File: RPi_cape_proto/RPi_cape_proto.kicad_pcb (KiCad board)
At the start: 2 copper layers, 104 x 172 mm, 206 parts, among them J1 Conn_01x04, J10 Conn_01x02, J11 Conn_01x02, J12 Conn_01x02, J14 Conn_01x02, J15 Conn_01x06, J16 Conn_01x06, J2 Conn_02x20_Odd_Even, J21 Conn_01x06, J3 Conn_01x02, J4 Conn_01x02, J5 Conn_02x20_Odd_Even, J7 Conn_01x02, J8 Conn_02x20_Odd_Even, J9 Conn_01x02, Q1 MMBT3904, Q11 MMBT3904, Q12 MMBT3906, Q13 MMBT3904, Q2 MMBT3904, Q3 MMBT3904, U18 74LVC1G08, U19 TPS1H100B, U2 ADC128D818, U20 74LVC1G08, U21 TPS1H100B, U22 74LVC1G08, U23 TPS1H100B, U28 LM4871M, U3 ADC128D818, U36 LMC7101B, U37 LMC7101B, U38 LMC7101B, U4 AD8552A, U8 74LVC1G08, U9 TPS1H100B

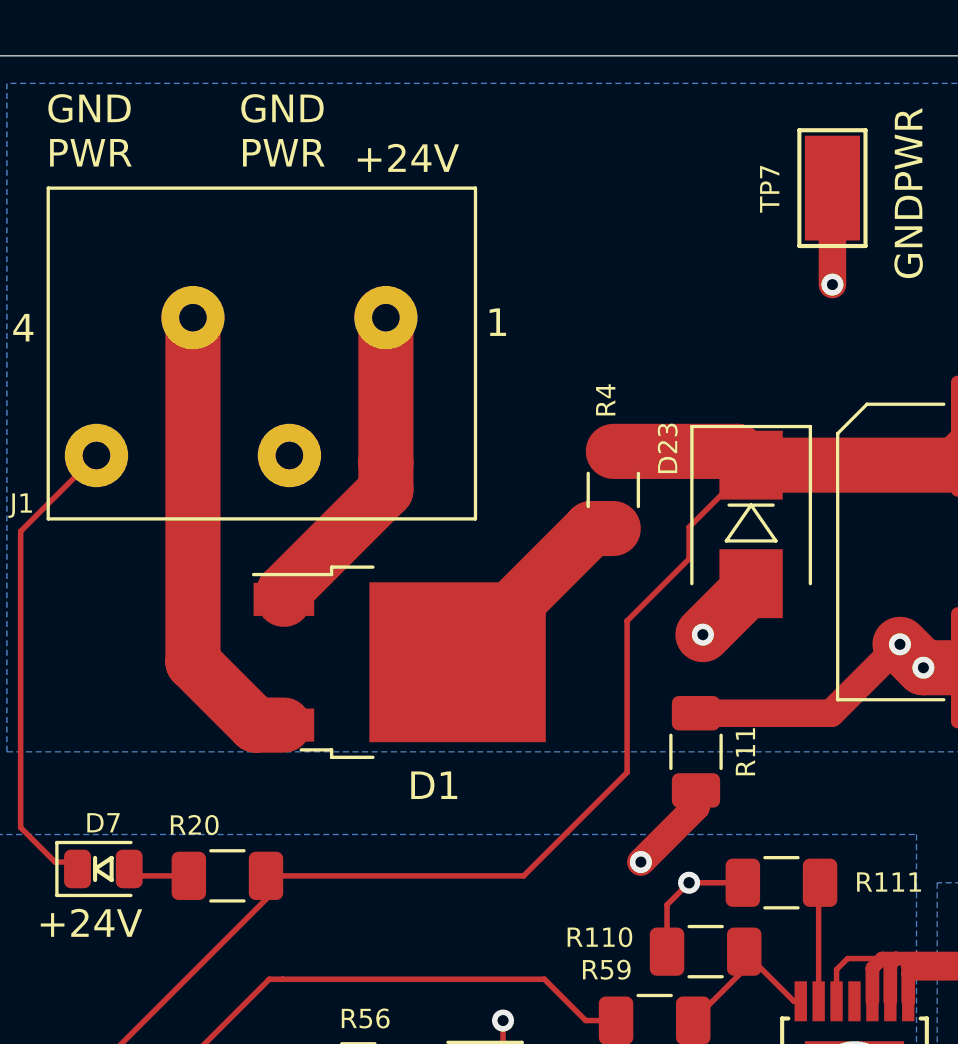
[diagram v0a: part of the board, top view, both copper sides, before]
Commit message: Input ORing-diode details
Changed part number and improved heatsinking for input power OR-ing diode
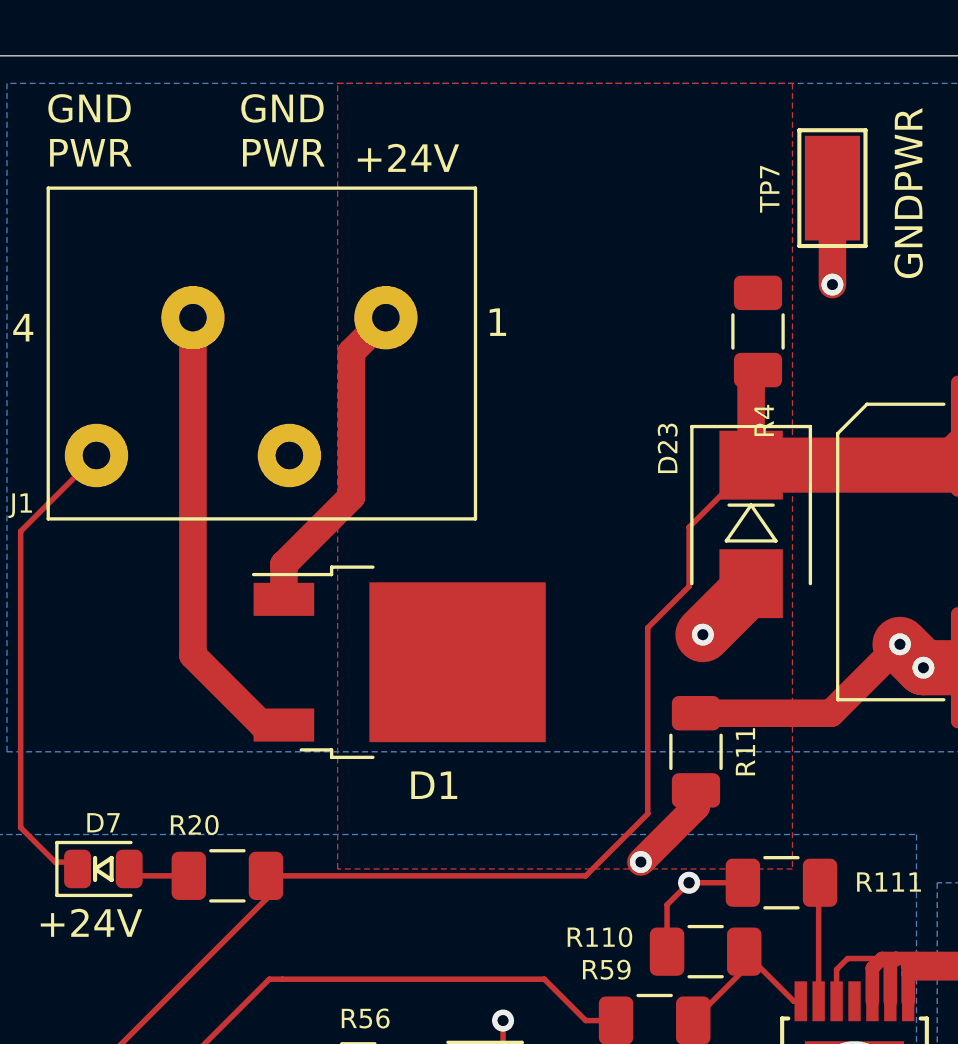
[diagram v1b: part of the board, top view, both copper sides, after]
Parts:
- moved R4 7.79 mm to (108.2, 121.5), turned to 270 degrees
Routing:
- net Net-(D1-Pad2): track 7.66 -> 0.00 mm
- added copper zone on F.Cu, net Net-(D1-Pad2)
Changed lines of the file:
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@@
     (thickness 1.6)
     (drawings 56)
-    (tracks 1412)
+    (tracks 1410)
     (zones 0)
     (modules 206)
@@
   )
   (setup
-    (last_trace_width 0.2)
+    (last_trace_width 1)
     (user_trace_width 0.2)
     (user_trace_width 0.25)
@@
     (mod_text_size 1 1)
     (mod_text_width 0.15)
-    (pad_size 5.35 8.54)
+    (pad_size 6.4 5.8)
     (pad_drill 0)
     (pad_to_mask_clearance 0.051)
@@
     (pad "" smd rect (at 3.775 1.525) (size 3.05 2.75) (layers F.Paste))
     (pad 2 smd rect (at 2.1 0) (size 6.4 5.8) (layers F.Cu F.Mask)
-      (net 27 "Net-(D1-Pad2)"))
+      (net 27 "Net-(D1-Pad2)") (zone_connect 2))
     (pad 3 smd rect (at -4.2 2.28) (size 2.2 1.2) (layers F.Cu F.Paste F.Mask)
       (net 209 "Net-(D1-Pad3)"))
@@
   )
   (module Resistor_SMD:R_1206_3216Metric (layer F.Cu)
-    (at 103 127.25 90)
+    (at 108.25 121.5 270)
     (descr "Resistor SMD 1206 (3216 Metric), square (rectangular) end terminal, IPC_7351 nominal, (Body size source: http://www.tortai-tech.com/upload/download/2011102023233369053.pdf), generated with kicad-footprint-generator")
     (tags resistor)
@@
     (fp_line (start -1.6 -0.8) (end 1.6 -0.8) (layer F.Fab) (width 0.1))
     (fp_line (start -1.6 0.8) (end -1.6 -0.8) (layer F.Fab) (width 0.1))
-    (pad 2 smd roundrect (at 1.4 0 90) (size 1.25 1.75) (layers F.Cu F.Paste F.Mask) (roundrect_rratio 0.2)
+    (pad 2 smd roundrect (at 1.4 0 270) (size 1.25 1.75) (layers F.Cu F.Paste F.Mask) (roundrect_rratio 0.2)
       (net 4 +24V))
-    (pad 1 smd roundrect (at -1.4 0 90) (size 1.25 1.75) (layers F.Cu F.Paste F.Mask) (roundrect_rratio 0.2)
+    (pad 1 smd roundrect (at -1.4 0 270) (size 1.25 1.75) (layers F.Cu F.Paste F.Mask) (roundrect_rratio 0.2)
       (net 27 "Net-(D1-Pad2)"))
     (model ${KISYS3DMOD}/Resistor_SMD.3dshapes/R_1206_3216Metric.wrl
@@
   (segment (start 128.45 124.95) (end 125.55 124.95) (width 0.25) (layer F.Cu) (net 4))
   (segment (start 125.55 124.95) (end 123.65 126.85) (width 0.25) (layer F.Cu) (net 4))
-  (segment (start 107.5 125.85) (end 108 126.35) (width 2) (layer F.Cu) (net 4))
-  (segment (start 103 125.85) (end 107.5 125.85) (width 2) (layer F.Cu) (net 4))
   (segment (start 90.4 142.1) (end 90.4 141.25) (width 0.2) (layer F.Cu) (net 4))
   (segment (start 75.3 158.5) (end 75.3 157.2) (width 0.2) (layer F.Cu) (net 4))
   (segment (start 75.3 157.2) (end 90.4 142.1) (width 0.2) (layer F.Cu) (net 4))
-  (segment (start 90.4 141.25) (end 99.75 141.25) (width 0.2) (layer F.Cu) (net 4))
-  (segment (start 99.75 141.25) (end 103.5 137.5) (width 0.2) (layer F.Cu) (net 4))
-  (segment (start 103.5 137.5) (end 103.5 132) (width 0.2) (layer F.Cu) (net 4))
-  (segment (start 103.5 132) (end 105.75 129.75) (width 0.2) (layer F.Cu) (net 4))
+  (segment (start 108 123.15) (end 108.15 123) (width 1) (layer F.Cu) (net 4))
+  (segment (start 108 126.35) (end 108 123.15) (width 1) (layer F.Cu) (net 4))
   (segment (start 105.75 128.6) (end 108 126.35) (width 0.2) (layer F.Cu) (net 4))
-  (segment (start 105.75 129.75) (end 105.75 128.6) (width 0.2) (layer F.Cu) (net 4))
+  (segment (start 105.75 130.75) (end 105.75 128.6) (width 0.2) (layer F.Cu) (net 4))
+  (segment (start 104.25 132.25) (end 105.75 130.75) (width 0.2) (layer F.Cu) (net 4))
+  (segment (start 104.25 139) (end 104.25 132.25) (width 0.2) (layer F.Cu) (net 4))
+  (segment (start 90.4 141.25) (end 102 141.25) (width 0.2) (layer F.Cu) (net 4))
+  (segment (start 102 141.25) (end 104.25 139) (width 0.2) (layer F.Cu) (net 4))
   (segment (start 71.125 189.25) (end 72.6875 190.8125) (width 1) (layer B.Cu) (net 5))
   (segment (start 70.5 189.25) (end 71.125 189.25) (width 1) (layer B.Cu) (net 5))
@@
   (segment (start 72.2 136.05) (end 74.25 138.1) (width 1) (layer F.Cu) (net 26))
   (segment (start 72.2 131.5) (end 72.2 136.05) (width 1) (layer F.Cu) (net 26))
-  (segment (start 102.2 128.65) (end 97.35 133.5) (width 2) (layer F.Cu) (net 27))
-  (segment (start 103 128.65) (end 102.2 128.65) (width 2) (layer F.Cu) (net 27))
-  (segment (start 94.75 126.25) (end 94.75 121) (width 2) (layer F.Cu) (net 28))
-  (segment (start 91.05 131.22) (end 91.05 130.95) (width 2) (layer F.Cu) (net 28))
-  (segment (start 94.75 127.25) (end 94.75 126.25) (width 2) (layer F.Cu) (net 28))
-  (segment (start 91.05 130.95) (end 94.75 127.25) (width 2) (layer F.Cu) (net 28))
+  (segment (start 91.05 131.22) (end 91.05 129.95) (width 1) (layer F.Cu) (net 28))
+  (segment (start 91.05 129.95) (end 93.5 127.5) (width 1) (layer F.Cu) (net 28))
+  (segment (start 93.5 122.25) (end 94.75 121) (width 1) (layer F.Cu) (net 28))
+  (segment (start 93.5 127.5) (end 93.5 122.25) (width 1) (layer F.Cu) (net 28))
   (segment (start 76.4625 140.9) (end 76.5 140.9375) (width 0.2) (layer F.Cu) (net 29))
   (segment (start 74.25 140.9) (end 76.4625 140.9) (width 0.2) (layer F.Cu) (net 29))
@@
   (segment (start 34.2 216.75) (end 34.04 216.91) (width 0.2) (layer B.Cu) (net 208))
   (segment (start 35.75 216.75) (end 34.2 216.75) (width 0.2) (layer B.Cu) (net 208))
-  (segment (start 91.05 135.78) (end 90.03 135.78) (width 2) (layer F.Cu) (net 209))
-  (segment (start 87.75 133.5) (end 87.75 121) (width 2) (layer F.Cu) (net 209))
-  (segment (start 90.03 135.78) (end 87.75 133.5) (width 2) (layer F.Cu) (net 209))
+  (segment (start 91.05 135.78) (end 90.28 135.78) (width 1) (layer F.Cu) (net 209))
+  (segment (start 87.75 133.25) (end 87.75 121) (width 1) (layer F.Cu) (net 209))
+  (segment (start 90.28 135.78) (end 87.75 133.25) (width 1) (layer F.Cu) (net 209))
   (zone (net 3) (net_name GNDPWR) (layer B.Cu) (hatch edge 0.508)
     (connect_pads (clearance 0.508))
@@
       )
     )
+  )
+  (zone (net 27) (net_name "Net-(D1-Pad2)") (layer F.Cu) (hatch edge 0.508)
+    (connect_pads (clearance 0.508))
+    (min_thickness 0.254)
+    (fill yes (arc_segments 32) (thermal_gap 0.508) (thermal_bridge_width 0.508))
+    (polygon
+      (pts
+        (xy 93 141) (xy 93 112.5) (xy 109.5 112.5) (xy 109.5 141)
+      )
+    )

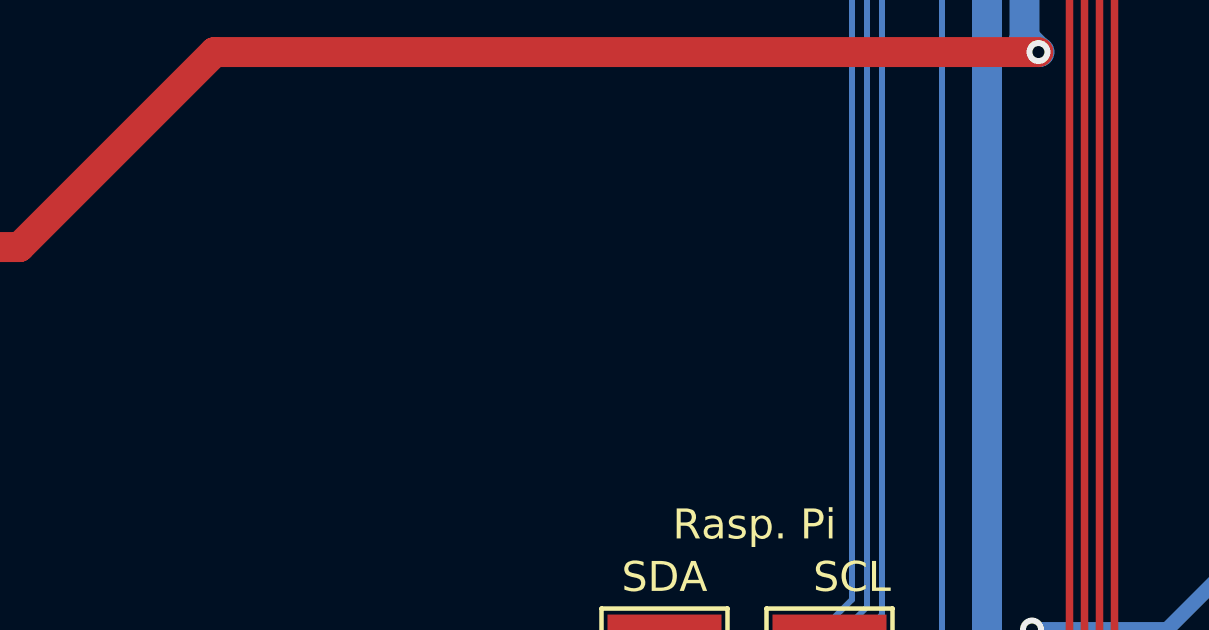
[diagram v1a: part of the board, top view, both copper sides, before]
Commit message: Admin (licensing, naming)
Put under CERN open hardware license
Changed name to GlobalVent
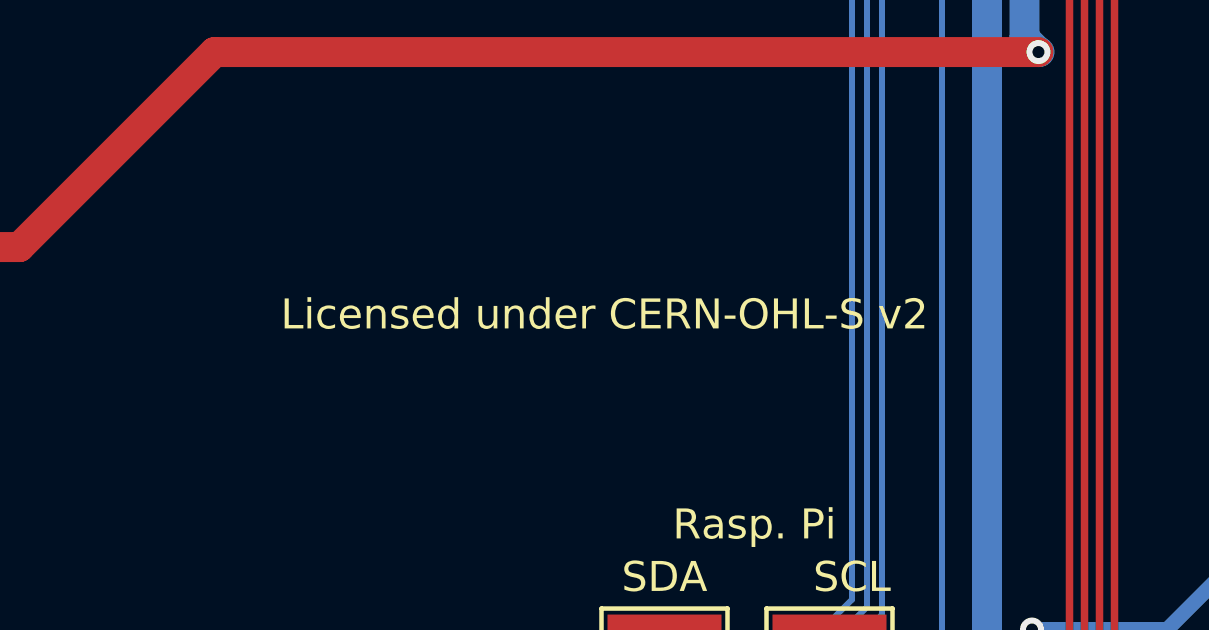
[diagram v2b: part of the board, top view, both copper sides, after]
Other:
- board text added: "Licensed under CERN-OHL-S v2"
